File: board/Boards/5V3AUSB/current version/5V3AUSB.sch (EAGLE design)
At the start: 14 parts

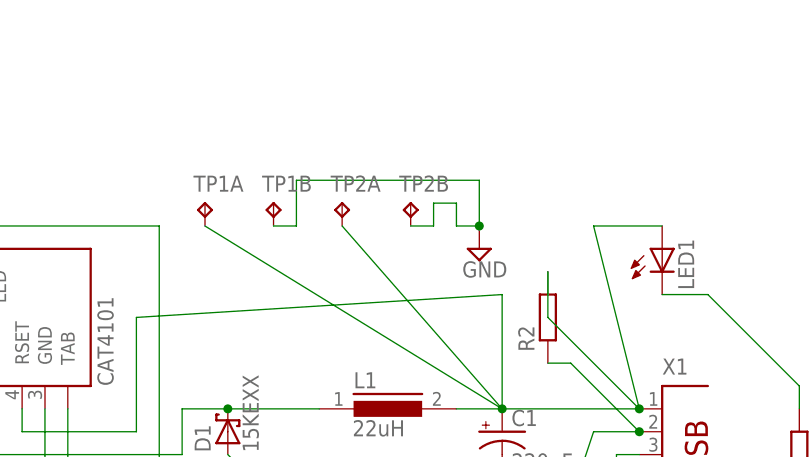
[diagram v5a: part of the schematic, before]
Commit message: added more outputs, board placement updated
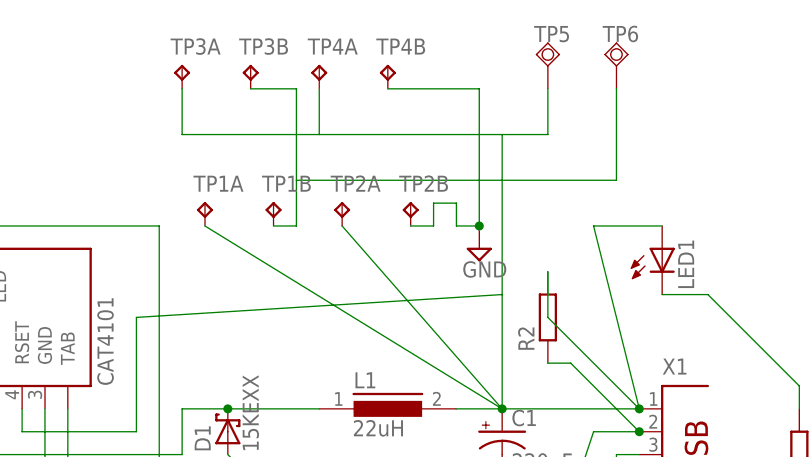
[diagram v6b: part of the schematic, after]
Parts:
- added TP3, TP4: TP2P2-38-20, testpad:TP2P2-38-20
- added TP5, TP6: TPSQTP20R, testpad:TPSQTP20R
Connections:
- net GND: now also TP3B.TP, TP4B.TP, TP6.TP
- net N$3: now also TP3A.TP, TP4A.TP, TP5.TP
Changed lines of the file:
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@@
 <part name="TP2" library="testpad" deviceset="TP2" device="P2-38-20"/>
 <part name="SUPPLY6" library="supply2" deviceset="GND" device=""/>
+<part name="TP3" library="testpad" deviceset="TP2" device="P2-38-20"/>
+<part name="TP4" library="testpad" deviceset="TP2" device="P2-38-20"/>
+<part name="TP5" library="testpad" deviceset="TPSQ" device="TP20R"/>
+<part name="TP6" library="testpad" deviceset="TPSQ" device="TP20R"/>
 </parts>
 <sheets>
@@
 <instance part="TP2" gate="B" x="109.22" y="127"/>
 <instance part="SUPPLY6" gate="GND" x="116.84" y="121.92"/>
+<instance part="TP3" gate="A" x="83.82" y="142.24"/>
+<instance part="TP3" gate="B" x="91.44" y="142.24"/>
+<instance part="TP4" gate="A" x="99.06" y="142.24"/>
+<instance part="TP4" gate="B" x="106.68" y="142.24"/>
+<instance part="TP5" gate="G$1" x="124.46" y="142.24" rot="R180"/>
+<instance part="TP6" gate="G$1" x="132.08" y="142.24" rot="R180"/>
 </instances>
 <busses>
@@
 <wire x1="114.3" y1="124.46" x2="116.84" y2="124.46" width="0.1524" layer="91"/>
 <junction x="116.84" y="124.46"/>
+<pinref part="TP6" gate="G$1" pin="TP"/>
+<wire x1="132.08" y1="139.7" x2="132.08" y2="129.54" width="0.1524" layer="91"/>
+<wire x1="132.08" y1="129.54" x2="116.84" y2="129.54" width="0.1524" layer="91"/>
+<pinref part="TP4" gate="B" pin="TP"/>
+<wire x1="116.84" y1="129.54" x2="116.84" y2="139.7" width="0.1524" layer="91"/>
+<wire x1="116.84" y1="139.7" x2="106.68" y2="139.7" width="0.1524" layer="91"/>
+<pinref part="TP3" gate="B" pin="TP"/>
+<wire x1="96.52" y1="129.54" x2="96.52" y2="139.7" width="0.1524" layer="91"/>
+<wire x1="96.52" y1="139.7" x2="91.44" y2="139.7" width="0.1524" layer="91"/>
 </segment>
 </net>
@@
 <junction x="119.38" y="104.14"/>
 <junction x="134.62" y="104.14"/>
+<pinref part="TP3" gate="A" pin="TP"/>
+<wire x1="83.82" y1="139.7" x2="83.82" y2="134.62" width="0.1524" layer="91"/>
+<wire x1="83.82" y1="134.62" x2="99.06" y2="134.62" width="0.1524" layer="91"/>
+<pinref part="TP4" gate="A" pin="TP"/>
+<wire x1="99.06" y1="134.62" x2="99.06" y2="139.7" width="0.1524" layer="91"/>
+<pinref part="TP5" gate="G$1" pin="TP"/>
+<wire x1="99.06" y1="134.62" x2="119.38" y2="134.62" width="0.1524" layer="91"/>
+<wire x1="119.38" y1="134.62" x2="124.46" y2="134.62" width="0.1524" layer="91"/>
+<wire x1="124.46" y1="134.62" x2="124.46" y2="139.7" width="0.1524" layer="91"/>
+<wire x1="119.38" y1="116.84" x2="119.38" y2="134.62" width="0.1524" layer="91"/>
 </segment>
 </net>
